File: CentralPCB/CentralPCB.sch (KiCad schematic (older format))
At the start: 53 parts, among them J1 POWER HEADER, J2 SPI Header, J3 Conn_02x16_Odd_Even, U1 AD8531, U2 Teensy4.1, U3 BA7810CP-E2

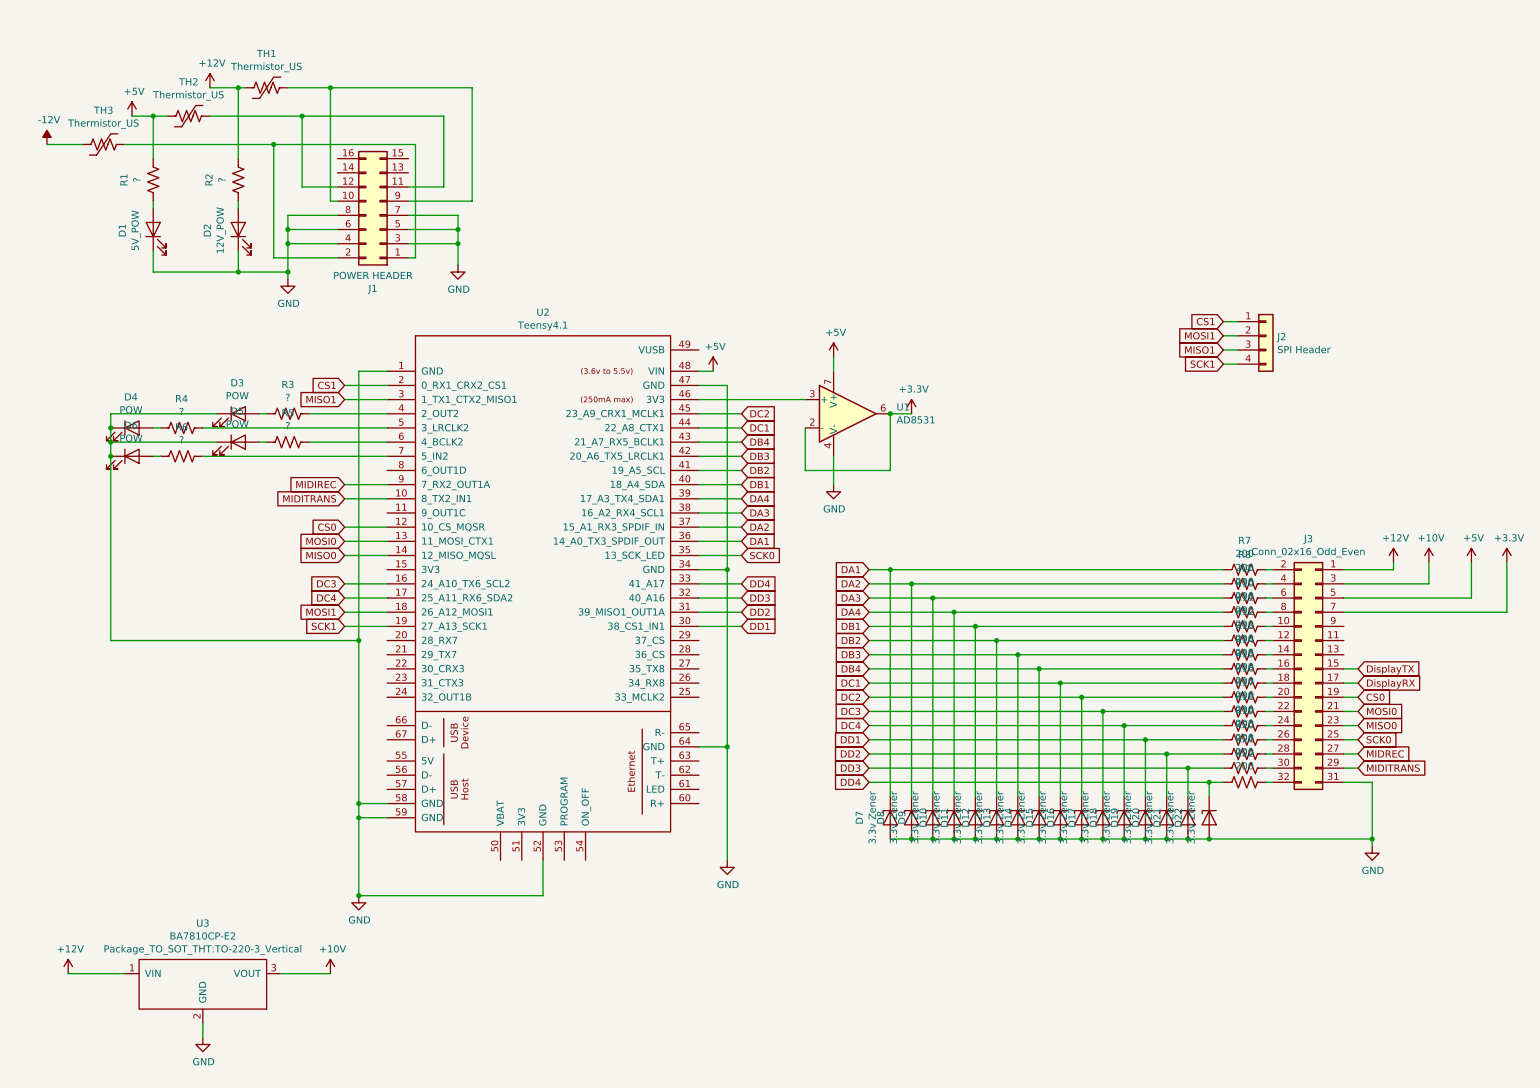
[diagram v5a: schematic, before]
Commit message: Updated DAC connections
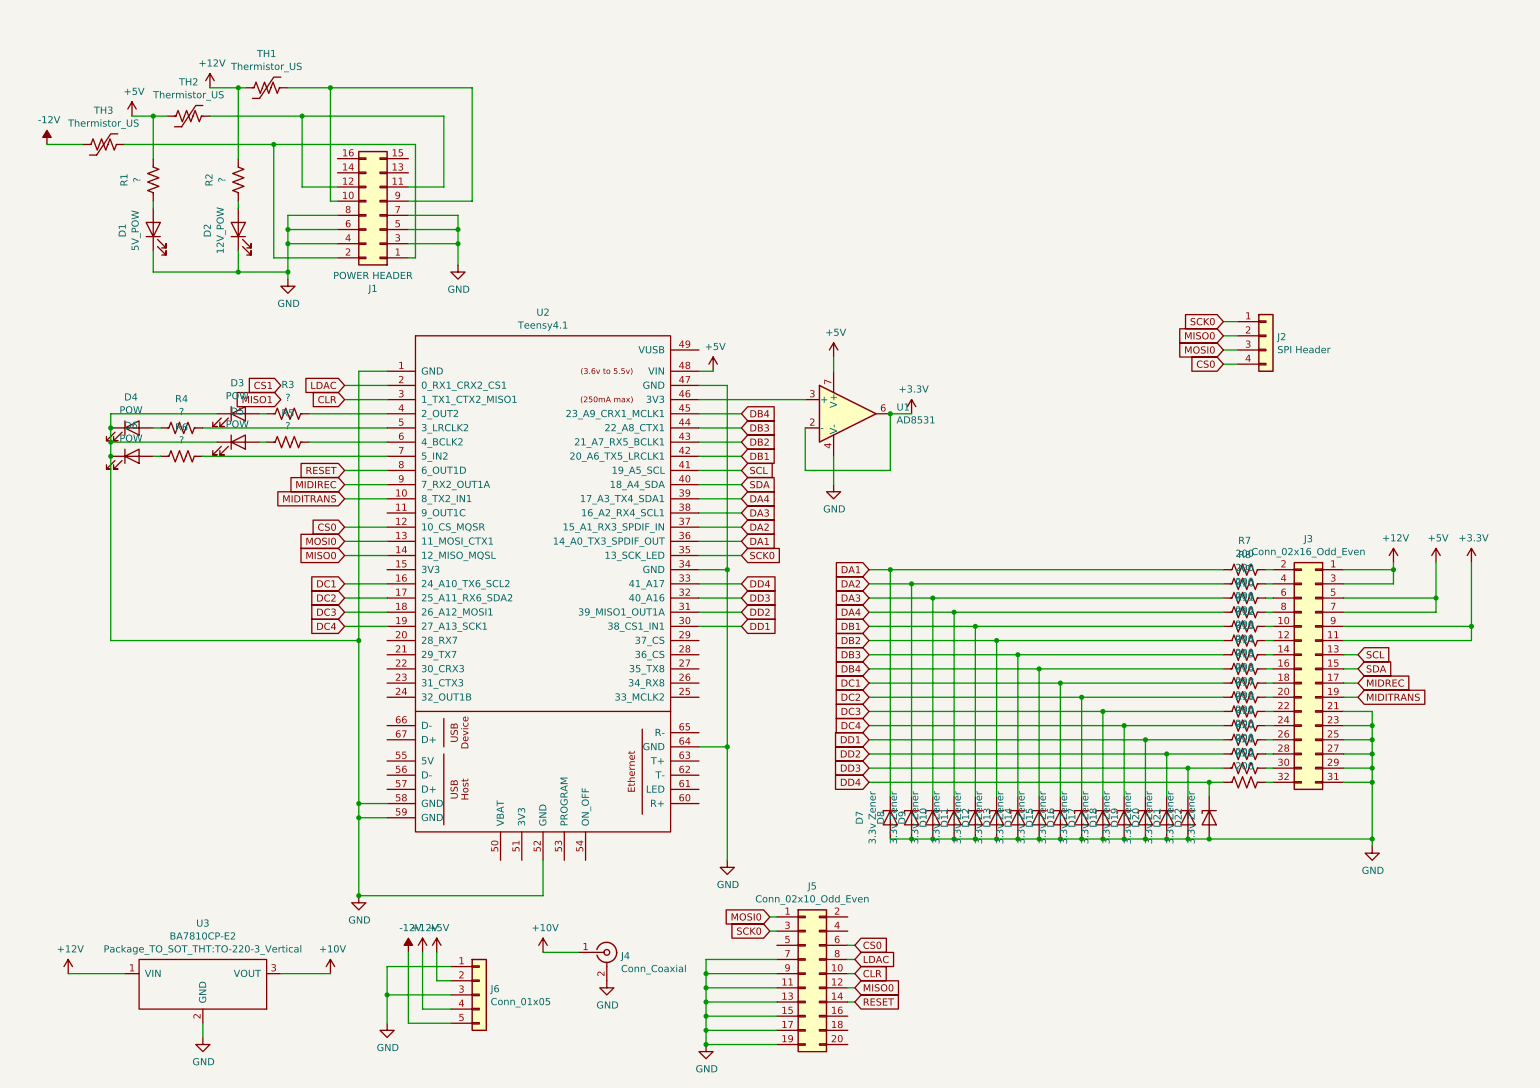
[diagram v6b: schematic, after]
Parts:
- added J4: Conn_Coaxial, Connector_Coaxial:SMB_Jack_Vertical, symbol Connector:Conn_Coaxial
- added J5: Conn_02x10_Odd_Even, Connector_PinSocket_2.54mm:PinSocket_2x10_P2.54mm_Vertical, symbol Connector_Generic:Conn_02x10_Odd_Even
- added J6: Conn_01x05, Connectors_Phoenix:PhoenixContact_MCV-G_05x3.50mm_Vertical, symbol Connector_Generic:Conn_01x05
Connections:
- net DisplayRX is gone; now on net MIDREC: J3.17 (Pin_17)
- net +10V: now also J4.1 (In); no longer J3.3 (Pin_3)
- net +12V: now also J3.3 (Pin_3), J6.4 (Pin_4)
- net +3V3: now also J3.11 (Pin_11), J3.9 (Pin_9); no longer J3.7 (Pin_7)
- net +5V: now also J3.7 (Pin_7), J6.2 (Pin_2)
- net -12V: now also J6.5 (Pin_5)
- net CS0: now also J2.4 (Pin_4), J5.6 (Pin_6); no longer J3.19 (Pin_19)
- net CS1: no longer J2.1 (Pin_1), U2.2 (0_RX1_CRX2_CS1)
- net DB1: now also U2.42 (20_A6_TX5_LRCLK1); no longer U2.40 (18_A4_SDA)
- net DB2: now also U2.43 (21_A7_RX5_BCLK1); no longer U2.41 (19_A5_SCL)
- net DB3: now also U2.44 (22_A8_CTX1); no longer U2.42 (20_A6_TX5_LRCLK1)
- net DB4: now also U2.45 (23_A9_CRX1_MCLK1); no longer U2.43 (21_A7_RX5_BCLK1)
- net DC1: now also U2.16 (24_A10_TX6_SCL2); no longer U2.44 (22_A8_CTX1)
- net DC2: now also U2.17 (25_A11_RX6_SDA2); no longer U2.45 (23_A9_CRX1_MCLK1)
- net DC3: now also U2.18 (26_A12_MOSI1); no longer U2.16 (24_A10_TX6_SCL2)
- net DC4: now also U2.19 (27_A13_SCK1); no longer U2.17 (25_A11_RX6_SDA2)
- net GND: now also J3.21 (Pin_21), J3.23 (Pin_23), J3.25 (Pin_25), J3.27 (Pin_27), J3.29 (Pin_29), J4.2 (Ext), J5.11 (Pin_11), J5.13 (Pin_13), J5.15 (Pin_15), J5.17 (Pin_17), J5.19 (Pin_19), J5.7 (Pin_7), J5.9 (Pin_9), J6.1 (Pin_1), J6.3 (Pin_3)
- net MIDITRANS: now also J3.19 (Pin_19); no longer J3.29 (Pin_29)
- net MIDREC: no longer J3.27 (Pin_27)
- net MISO0: now also J2.2 (Pin_2), J5.12 (Pin_12); no longer J3.23 (Pin_23)
- net MISO1: no longer J2.3 (Pin_3), U2.3 (1_TX1_CTX2_MISO1)
- net MOSI0: now also J2.3 (Pin_3), J5.1 (Pin_1); no longer J3.21 (Pin_21)
- net SCK0: now also J2.1 (Pin_1), J5.3 (Pin_3); no longer J3.25 (Pin_25)
- net SCL: now reaches J3.13 (Pin_13)
- net SCL: now also U2.41 (19_A5_SCL)
- net RESET: now reaches U2.8 (6_OUT1D)
- net RESET: now also J5.14 (Pin_14)
- net DisplayTX renamed SDA
- net SDA: now also U2.40 (18_A4_SDA)
- removed net MOSI1: J2.2 (Pin_2), U2.18 (26_A12_MOSI1)
- removed net SCK1: J2.4 (Pin_4), U2.19 (27_A13_SCK1)
- new net CLR: J5.10 (Pin_10), U2.3 (1_TX1_CTX2_MISO1)
- new net LDAC: J5.8 (Pin_8), U2.2 (0_RX1_CRX2_CS1)

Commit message: Pin updates
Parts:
- added J? (x2): Conn_01x24, Connector_PinSocket_2.54mm:PinSocket_1x23_P2.54mm_Vertical, symbol Connector_Generic:Conn_01x24
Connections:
- net +5V: now also J?.1 (Pin_1)
- net CLR: now also U2.24 (32_OUT1B), J?.24 (Pin_24); no longer U2.3 (1_TX1_CTX2_MISO1)
- net CS0: now also J?.12 (Pin_12)
- net DA1: now also J?.13 (Pin_13)
- net DA2: now also J?.12 (Pin_12)
- net DA3: now also J?.11 (Pin_11)
- net DA4: now also J?.10 (Pin_10)
- net DB1: now also J?.7 (Pin_7)
- net DB2: now also J?.6 (Pin_6)
- net DB3: now also J?.5 (Pin_5)
- net DB4: now also J?.4 (Pin_4)
- net DC1: now also J?.16 (Pin_16)
- net DC2: now also J?.17 (Pin_17)
- net DC3: now also J?.18 (Pin_18)
- net DC4: now also J?.19 (Pin_19)
- net DD1: now also J?.19 (Pin_19)
- net DD2: now also J?.18 (Pin_18)
- net DD3: now also J?.17 (Pin_17)
- net DD4: now also J?.16 (Pin_16)
- net GND: now also J?.1 (Pin_1), J?.15 (Pin_15), J?.2 (Pin_2)
- net LDAC: now also U2.23 (31_CTX3), J?.23 (Pin_23); no longer U2.2 (0_RX1_CRX2_CS1)
- net MIDIREC: now also J?.9 (Pin_9)
- net MIDITRANS: now also J?.10 (Pin_10)
- net MISO0: now also J?.14 (Pin_14)
- net MOSI0: now also J?.13 (Pin_13)
- net RESET: now also U2.22 (30_CRX3), J?.22 (Pin_22); no longer U2.8 (6_OUT1D)
- net SCK0: now also J?.14 (Pin_14)
- net SCL: now also J?.8 (Pin_8)
- net SDA: now also J?.9 (Pin_9)
- net at R3.1, U2.4 (2_OUT2): now also J?.4 (Pin_4)
- net at R4.1, U2.5 (3_LRCLK2): now also J?.5 (Pin_5)
- net at R5.1, U2.6 (4_BCLK2): now also J?.6 (Pin_6)
- net at R6.1, U2.7 (5_IN2): now also J?.7 (Pin_7)
- net at U2.11 (9_OUT1C): now also J?.11 (Pin_11)
- net at U2.15 (3V3): now also J?.15 (Pin_15)
- net at U2.20 (28_RX7): now also J?.20 (Pin_20)
- net at U2.21 (29_TX7): now also J?.21 (Pin_21)
- net at U2.25 (33_MCLK2): now also J?.24 (Pin_24)
- net at U2.26 (34_RX8): now also J?.23 (Pin_23)
- net at U2.27 (35_TX8): now also J?.22 (Pin_22)
- net at U2.28 (36_CS): now also J?.21 (Pin_21)
- net at U2.29 (37_CS): now also J?.20 (Pin_20)
- net at U1.3 (+), U2.46 (3V3): now also J?.3 (Pin_3)
- new net: J?.2 (Pin_2), U2.2 (0_RX1_CRX2_CS1)
- new net: J?.3 (Pin_3), U2.3 (1_TX1_CTX2_MISO1)
- new net: J?.8 (Pin_8), U2.8 (6_OUT1D)
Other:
- moved on the sheet: D3, D4, D5, D6, R3, R4, R5, R6, U1

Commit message: small pcb changes
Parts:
- added D?: -12V_pow, LED_THT:LED_D3.0mm, symbol Device:LED
- added R?: ?, Resistor_SMD:R_0805_2012Metric, symbol Device:R_US
- U2: symbol teensy:Teensy4.1 -> CentralPCB-rescue:Teensy4.1-teensy
- U3: symbol test-lib:BA7810CP-E2 -> CentralPCB-rescue:BA7810CP-E2-test-lib
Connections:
- net +12V: now also U1.7 (V+)
- net +5V: no longer U1.7 (V+)
- net -12V: now also U1.4 (V-)
- net GND: now also D?.2 (A); no longer U1.4 (V-)
- net at J1.1 (Pin_1), J1.2 (Pin_2), TH3.1: now also R?.1
- new net: D?.1 (K), R?.2
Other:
- moved on the sheet: TH3
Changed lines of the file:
@@
 EESchema Schematic File Version 4
+LIBS:CentralPCB-cache
 EELAYER 30 0
 EELAYER END
@@
 L power:-12V #PWR03
 U 1 1 6162992E
-P 700 1200
-F 0 "#PWR03" H 700 1300 50  0001 C CNN
-F 1 "-12V" H 715 1373 50  0000 C CNN
-F 2 "" H 700 1200 50  0001 C CNN
-F 3 "" H 700 1200 50  0001 C CNN
-	1    700  1200
+P 550 1200
+F 0 "#PWR03" H 550 1300 50  0001 C CNN
+F 1 "-12V" H 565 1373 50  0000 C CNN
+F 2 "" H 550 1200 50  0001 C CNN
+F 3 "" H 550 1200 50  0001 C CNN
+	1    550  1200
 	1    0    0    -1
 $EndComp
@@
 $EndComp
 $Comp
-L test-lib:BA7810CP-E2 U3
+L CentralPCB-rescue:BA7810CP-E2-test-lib U3
 U 1 1 61610C90
 P 1800 7050
@@
 L Device:Thermistor_US TH3
 U 1 1 619DA6B6
-P 1100 1200
-F 0 "TH3" V 860 1200 50  0000 C CNN
-F 1 "Thermistor_US" V 951 1200 50  0000 C CNN
-F 2 "Resistor_SMD:R_1206_3216Metric" H 1100 1200 50  0001 C CNN
-F 3 "~" H 1100 1200 50  0001 C CNN
-	1    1100 1200
+P 950 1200
+F 0 "TH3" V 710 1200 50  0000 C CNN
+F 1 "Thermistor_US" V 801 1200 50  0000 C CNN
+F 2 "Resistor_SMD:R_1206_3216Metric" H 950 1200 50  0001 C CNN
+F 3 "~" H 950 1200 50  0001 C CNN
+	1    950  1200
 	0    1    1    0
 $EndComp
@@
 U 1 1 61C7A0EA
 P 1450 1800
-F 0 "D1" H 1443 2017 50  0000 C CNN
-F 1 "5V_POW" H 1443 1926 50  0000 C CNN
+F 0 "D1" V 1650 1700 50  0000 C CNN
+F 1 "5V_POW" V 1550 1600 50  0000 C CNN
 F 2 "LED_THT:LED_D3.0mm" H 1450 1800 50  0001 C CNN
 F 3 "~" H 1450 1800 50  0001 C CNN
@@
 U 1 1 6224F6A1
 P 2050 1800
-F 0 "D2" H 2043 2017 50  0000 C CNN
-F 1 "12V_POW" H 2043 1926 50  0000 C CNN
+F 0 "D2" V 1950 1950 50  0000 C CNN
+F 1 "12V_POW" V 1850 1950 50  0000 C CNN
 F 2 "LED_THT:LED_D3.0mm" H 2050 1800 50  0001 C CNN
 F 3 "~" H 2050 1800 50  0001 C CNN
@@
 $EndComp
 $Comp
-L power:+5V #PWR06
-U 1 1 6222D058
-P 6450 2700
-F 0 "#PWR06" H 6450 2550 50  0001 C CNN
-F 1 "+5V" H 6465 2873 50  0000 C CNN
-F 2 "" H 6450 2700 50  0001 C CNN
-F 3 "" H 6450 2700 50  0001 C CNN
-	1    6450 2700
-	1    0    0    -1
-$EndComp
-$Comp
-L power:GND #PWR09
-U 1 1 62205F7A
-P 6450 3600
-F 0 "#PWR09" H 6450 3350 50  0001 C CNN
-F 1 "GND" H 6455 3427 50  0000 C CNN
-F 2 "" H 6450 3600 50  0001 C CNN
-F 3 "" H 6450 3600 50  0001 C CNN
-	1    6450 3600
-	1    0    0    -1
-$EndComp
-$Comp
 L Amplifier_Operational:OP179GS U1
 U 1 1 621C9E2B
@@
 Connection ~ 3050 5850
 Wire Wire Line
-	5350 4200 5350 5450
-Wire Wire Line
 	5350 5450 5350 6250
 Wire Wire Line
@@
 Wire Wire Line
 	2400 1900 2400 2100
-Wire Wire Line
-	1250 1200 2300 1200
 Connection ~ 2300 1200
 Wire Wire Line
@@
 	2050 1600 2050 1650
 Wire Wire Line
-	700  1200 950  1200
+	550  1200 800  1200
 Connection ~ 2700 800
 Wire Wire Line
@@
 	3250 2000 3300 2000
 $Comp
-L teensy:Teensy4.1 U2
+L CentralPCB-rescue:Teensy4.1-teensy U2
 U 1 1 61AF984C
 P 4200 4950
@@
 $EndComp
 Wire Wire Line
-	5300 2800 5400 2800
-Wire Wire Line
 	3050 2800 3050 5200
 $Comp
@@
 Connection ~ 5350 5450
 Connection ~ 5350 4200
+Wire Wire Line
+	5400 2900 5350 2900
+Connection ~ 5350 2900
+Wire Wire Line
+	5400 4200 5350 4200
+$Comp
+L power:+12V #PWR?
+U 1 1 617B4C75
+P 6450 2700
+F 0 "#PWR?" H 6450 2550 50  0001 C CNN
+F 1 "+12V" H 6465 2873 50  0000 C CNN
+F 2 "" H 6450 2700 50  0001 C CNN
+F 3 "" H 6450 2700 50  0001 C CNN
+	1    6450 2700
+	1    0    0    -1
+$EndComp
+$Comp
+L power:-12V #PWR?
+U 1 1 617F806C
+P 6450 3600
+F 0 "#PWR?" H 6450 3700 50  0001 C CNN
+F 1 "-12V" H 6465 3773 50  0000 C CNN
+F 2 "" H 6450 3600 50  0001 C CNN
+F 3 "" H 6450 3600 50  0001 C CNN
+	1    6450 3600
+	-1   0    0    1
+$EndComp
+Connection ~ 5400 4600
+Wire Wire Line
+	5950 4600 5400 4600
+Connection ~ 5400 4500
+Wire Wire Line
+	5950 4500 5400 4500
+Connection ~ 5400 4400
+Wire Wire Line
+	5950 4400 5400 4400
+Connection ~ 5400 4300
+Wire Wire Line
+	5950 4300 5400 4300
+Connection ~ 5400 4100
+Wire Wire Line
+	5950 4100 5400 4100
+Connection ~ 5400 4000
+Wire Wire Line
+	5950 4000 5400 4000
+Connection ~ 5400 3900
+Wire Wire Line
+	5400 3900 5950 3900
+Connection ~ 5400 3800
+Wire Wire Line
+	5400 3800 5950 3800
+Connection ~ 5400 3700
+Wire Wire Line
+	5400 3700 5950 3700
+Connection ~ 5400 3600
+Wire Wire Line
+	5950 3600 5400 3600
+Connection ~ 5400 3500
+Wire Wire Line
+	5950 3500 5400 3500
+Connection ~ 5400 3400
+Wire Wire Line
+	5400 3400 5950 3400
+Connection ~ 5400 3300
+Wire Wire Line
+	5950 3300 5400 3300
+Connection ~ 5400 3200
+Wire Wire Line
+	5400 3200 5950 3200
+Connection ~ 5400 3100
+Wire Wire Line
+	5950 3100 5400 3100
+Connection ~ 5400 3000
+Wire Wire Line
+	5400 3000 6250 3000
+Connection ~ 5400 2800
+Wire Wire Line
+	5800 2800 5400 2800
+Wire Wire Line
+	5300 5100 5400 5100
+Wire Wire Line
+	5300 5000 5400 5000
+Wire Wire Line
+	5300 4900 5400 4900
+Wire Wire Line
+	5300 4800 5400 4800
+Wire Wire Line
+	5300 4700 5400 4700
+Wire Wire Line
+	5300 4600 5400 4600
+Wire Wire Line
+	5300 4500 5400 4500
+Wire Wire Line
+	5300 4400 5400 4400
+Wire Wire Line
+	5300 4300 5400 4300
+Wire Wire Line
+	5300 4100 5400 4100
+Wire Wire Line
+	5300 4000 5400 4000
+Wire Wire Line
+	5300 3900 5400 3900
+Wire Wire Line
+	5300 3800 5400 3800
+Wire Wire Line
+	5300 3700 5400 3700
+Wire Wire Line
+	5300 3600 5400 3600
+Wire Wire Line
+	5300 3500 5400 3500
+Wire Wire Line
+	5400 3400 5300 3400
+Wire Wire Line
+	5300 3300 5400 3300
+Wire Wire Line
+	5300 3200 5400 3200
+Wire Wire Line
+	5300 3100 5400 3100
+Wire Wire Line
+	5300 3000 5400 3000
+Wire Wire Line
+	5300 2800 5400 2800
+Wire Wire Line
+	5350 4200 5350 5450
+Wire Wire Line
+	5350 2900 5350 4200
 $Comp
 L Connector_Generic:Conn_01x24 J?
@@
 $EndComp
 Wire Wire Line
-	5800 2800 5400 2800
-Connection ~ 5400 2800
-Wire Wire Line
-	5400 2900 5350 2900
-Connection ~ 5350 2900
-Wire Wire Line
-	5400 3000 6250 3000
-Wire Wire Line
-	5300 3000 5400 3000
-Connection ~ 5400 3000
-Wire Wire Line
-	5300 3100 5400 3100
-Wire Wire Line
-	5950 3100 5400 3100
-Connection ~ 5400 3100
-Wire Wire Line
-	5300 3200 5400 3200
-Wire Wire Line
-	5400 3200 5950 3200
-Connection ~ 5400 3200
-Wire Wire Line
-	5300 3300 5400 3300
-Wire Wire Line
-	5950 3300 5400 3300
-Connection ~ 5400 3300
-Wire Wire Line
-	5400 3400 5300 3400
-Wire Wire Line
-	5400 3400 5950 3400
-Connection ~ 5400 3400
-Wire Wire Line
-	5300 3500 5400 3500
-Wire Wire Line
-	5950 3500 5400 3500
-Connection ~ 5400 3500
-Wire Wire Line
-	5950 3600 5400 3600
-Wire Wire Line
-	5300 3600 5400 3600
-Connection ~ 5400 3600
-Wire Wire Line
-	5300 3700 5400 3700
-Wire Wire Line
-	5400 3700 5950 3700
-Connection ~ 5400 3700
-Wire Wire Line
-	5300 3800 5400 3800
-Wire Wire Line
-	5400 3800 5950 3800
-Connection ~ 5400 3800
-Wire Wire Line
-	5300 3900 5400 3900
-Wire Wire Line
-	5400 3900 5950 3900
-Connection ~ 5400 3900
-Wire Wire Line
-	5350 2900 5350 4200
-Wire Wire Line
-	5300 4000 5400 4000
-Wire Wire Line
-	5950 4000 5400 4000
-Connection ~ 5400 4000
-Wire Wire Line
-	5300 4100 5400 4100
-Wire Wire Line
-	5950 4100 5400 4100
-Connection ~ 5400 4100
-Wire Wire Line
-	5400 4200 5350 4200
-Wire Wire Line
-	5300 4300 5400 4300
-Wire Wire Line
-	5300 4400 5400 4400
-Wire Wire Line
-	5300 4500 5400 4500
-Wire Wire Line
-	5300 4600 5400 4600
-Wire Wire Line
-	5300 4700 5400 4700
-Wire Wire Line
-	5300 4800 5400 4800
-Wire Wire Line
-	5300 4900 5400 4900
-Wire Wire Line
-	5300 5000 5400 5000
-Wire Wire Line
-	5300 5100 5400 5100
-Wire Wire Line
-	5950 4300 5400 4300
-Connection ~ 5400 4300
-Wire Wire Line
-	5950 4400 5400 4400
-Connection ~ 5400 4400
-Wire Wire Line
-	5950 4500 5400 4500
-Connection ~ 5400 4500
-Wire Wire Line
-	5950 4600 5400 4600
-Connection ~ 5400 4600
+	1100 1200 2300 1200
+$Comp
+L Device:LED D?
+U 1 1 618879C9
+P 1100 1950
+F 0 "D?" V 1100 1800 50  0000 C CNN
+F 1 "-12V_pow" V 1200 1750 50  0000 C CNN
+F 2 "LED_THT:LED_D3.0mm" H 1100 1950 50  0001 C CNN
+F 3 "~" H 1100 1950 50  0001 C CNN
+	1    1100 1950
+	0    1    1    0
+$EndComp
+Wire Wire Line
+	1100 1450 1100 1200
+Connection ~ 1100 1200
+Wire Wire Line
+	1100 1950 1100 2100
+Wire Wire Line
+	1100 2100 1450 2100
+Connection ~ 1450 2100
+Connection ~ 1100 2100
+$Comp
+L Device:R_US R?
+U 1 1 6197A5BF
+P 1100 1600
+F 0 "R?" V 895 1600 50  0000 C CNN
+F 1 "?" V 986 1600 50  0000 C CNN
+F 2 "Resistor_SMD:R_0805_2012Metric" V 1140 1590 50  0001 C CNN
+F 3 "~" H 1100 1600 50  0001 C CNN
+	1    1100 1600
+	1    0    0    -1
+$EndComp
+Wire Wire Line
+	1100 1750 1100 1800
 $EndSCHEMATC
